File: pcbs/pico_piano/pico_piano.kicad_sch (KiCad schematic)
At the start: 22 parts, among them U1 Pico

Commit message: WIP: real hardware tests
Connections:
- net A: now also U1.24 (GPIO18); no longer U1.22 (GPIO17)
- net AIS: now also U1.22 (GPIO17); no longer U1.24 (GPIO18)
- net B: now also U1.21 (GPIO16); no longer U1.25 (GPIO19)
- net GIS: now also U1.25 (GPIO19); no longer U1.21 (GPIO16)
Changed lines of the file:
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@@
 	)
 	(label "A"
-		(at 91.44 113.03 0)
+		(at 91.44 107.95 0)
 		(fields_autoplaced yes)
 		(effects
@@
 	)
 	(label "GIS"
-		(at 91.44 115.57 0)
+		(at 91.44 105.41 0)
 		(fields_autoplaced yes)
 		(effects
@@
 	)
 	(label "AIS"
-		(at 91.44 107.95 0)
+		(at 91.44 113.03 0)
 		(fields_autoplaced yes)
 		(effects
@@
 	)
 	(label "B"
-		(at 91.44 105.41 0)
+		(at 91.44 115.57 0)
 		(fields_autoplaced yes)
 		(effects

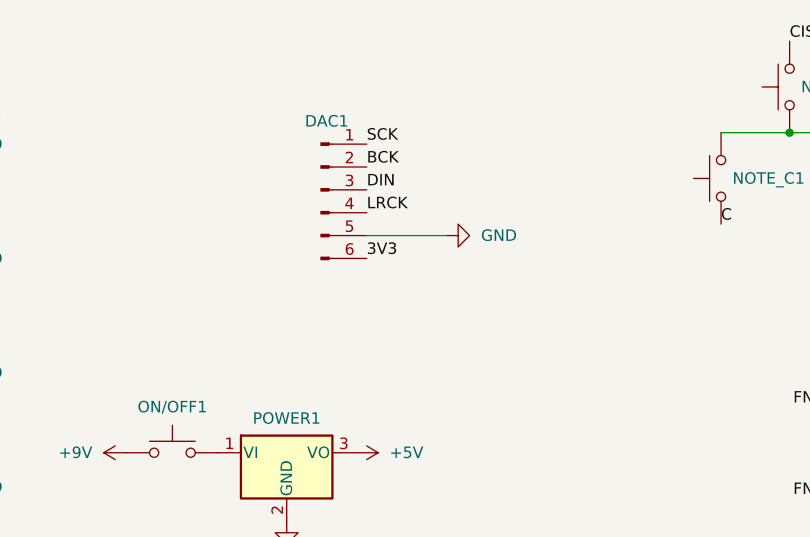
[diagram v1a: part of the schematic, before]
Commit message: Pico Piano PCB changes
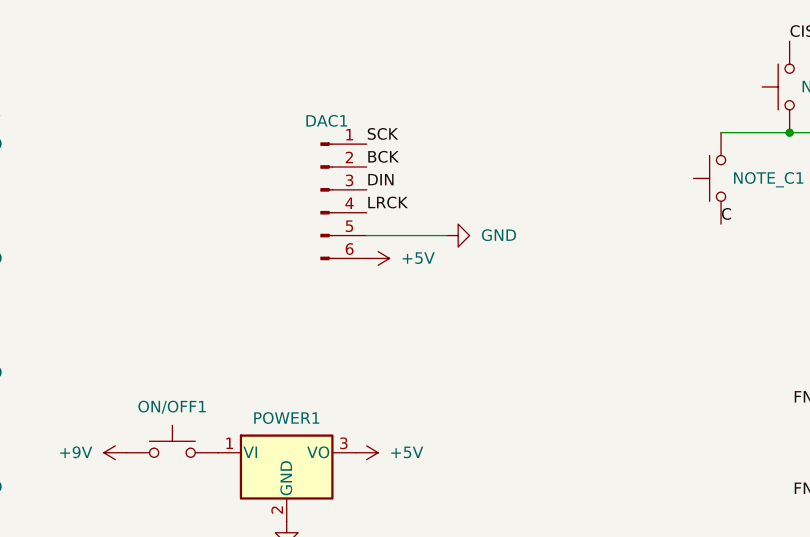
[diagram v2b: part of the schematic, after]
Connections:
- net +5V: now also DAC1.6 (Pin_6)
- net 3V3: no longer DAC1.6 (Pin_6)
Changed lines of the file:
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@@
 		)
 	)
-	(label "3V3"
-		(at 139.7 85.09 0)
+	(label "G"
+		(at 55.88 115.57 180)
 		(fields_autoplaced yes)
 		(effects
@@
 				(size 1.27 1.27)
 			)
-			(justify left bottom)
-		)
-	)
-	(label "G"
-		(at 55.88 115.57 180)
+			(justify right bottom)
+		)
+	)
+	(label "DIS"
+		(at 201.93 60.96 0)
 		(fields_autoplaced yes)
 		(effects
@@
 				(size 1.27 1.27)
 			)
-			(justify right bottom)
-		)
-	)
-	(label "DIS"
-		(at 201.93 60.96 0)
+			(justify left bottom)
+		)
+	)
+	(label "AIS"
+		(at 264.16 60.96 0)
 		(fields_autoplaced yes)
 		(effects
@@
 		)
 	)
-	(label "AIS"
-		(at 264.16 60.96 0)
+	(label "FIS"
+		(at 233.68 60.96 0)
 		(fields_autoplaced yes)
 		(effects
@@
 	)
 	(label "FIS"
-		(at 233.68 60.96 0)
+		(at 55.88 113.03 180)
 		(fields_autoplaced yes)
 		(effects
@@
 				(size 1.27 1.27)
 			)
-			(justify left bottom)
-		)
-	)
-	(label "FIS"
-		(at 55.88 113.03 180)
-		(fields_autoplaced yes)
-		(effects
-			(font
-				(size 1.27 1.27)
-			)
 			(justify right bottom)
 		)
@@
 					(unit 1)
 				)
+			)
+		)
+	)
+	(symbol
+		(lib_id "power:+5V")
+		(at 139.7 85.09 270)
+		(unit 1)
+		(exclude_from_sim no)
+		(in_bom yes)
+		(on_board yes)
+		(dnp no)
+		(fields_autoplaced yes)
+		(property "Reference" "#PWR018"
+			(at 135.89 85.09 0)
+			(effects
+				(font
+					(size 1.27 1.27)
+				)
+				(hide yes)
+			)
+		)
+		(property "Value" "+5V"
+			(at 143.51 85.0899 90)
+			(effects
+				(font
+					(size 1.27 1.27)
+				)
+				(justify left)
+			)
+		)
+		(property "Footprint" ""
+			(at 139.7 85.09 0)
+			(effects
+				(font
+					(size 1.27 1.27)
+				)
+				(hide yes)
+			)
+		)
+		(property "Datasheet" ""
+			(at 139.7 85.09 0)
+			(effects
+				(font
+					(size 1.27 1.27)
+				)
+				(hide yes)
+			)
+		)
+		(property "Description" "Power symbol creates a global label with name \"+5V\""
+			(at 139.7 85.09 0)
+			(effects
+				(font
+					(size 1.27 1.27)
+				)
+				(hide yes)
+			)
+		)
+		(pin "1"
+		)
+		(instances
+			(project ""
+				(path "/5e24b6d7-8d67-4f70-8e44-f3ac3114fe70"
+					(reference "#PWR018")
+					(unit 1)
+				)

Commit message: Update pico piano PCB
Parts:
- POWER1: footprint Package_TO_SOT_THT:TO-220-3_Vertical -> Package_TO_SOT_THT:TO-220-3_Horizontal_TabDown
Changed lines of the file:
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@@
 			)
 		)
-		(property "Footprint" "Package_TO_SOT_THT:TO-220-3_Vertical"
+		(property "Footprint" "Package_TO_SOT_THT:TO-220-3_Horizontal_TabDown"
 			(at 130.81 100.965 0)
 			(effects

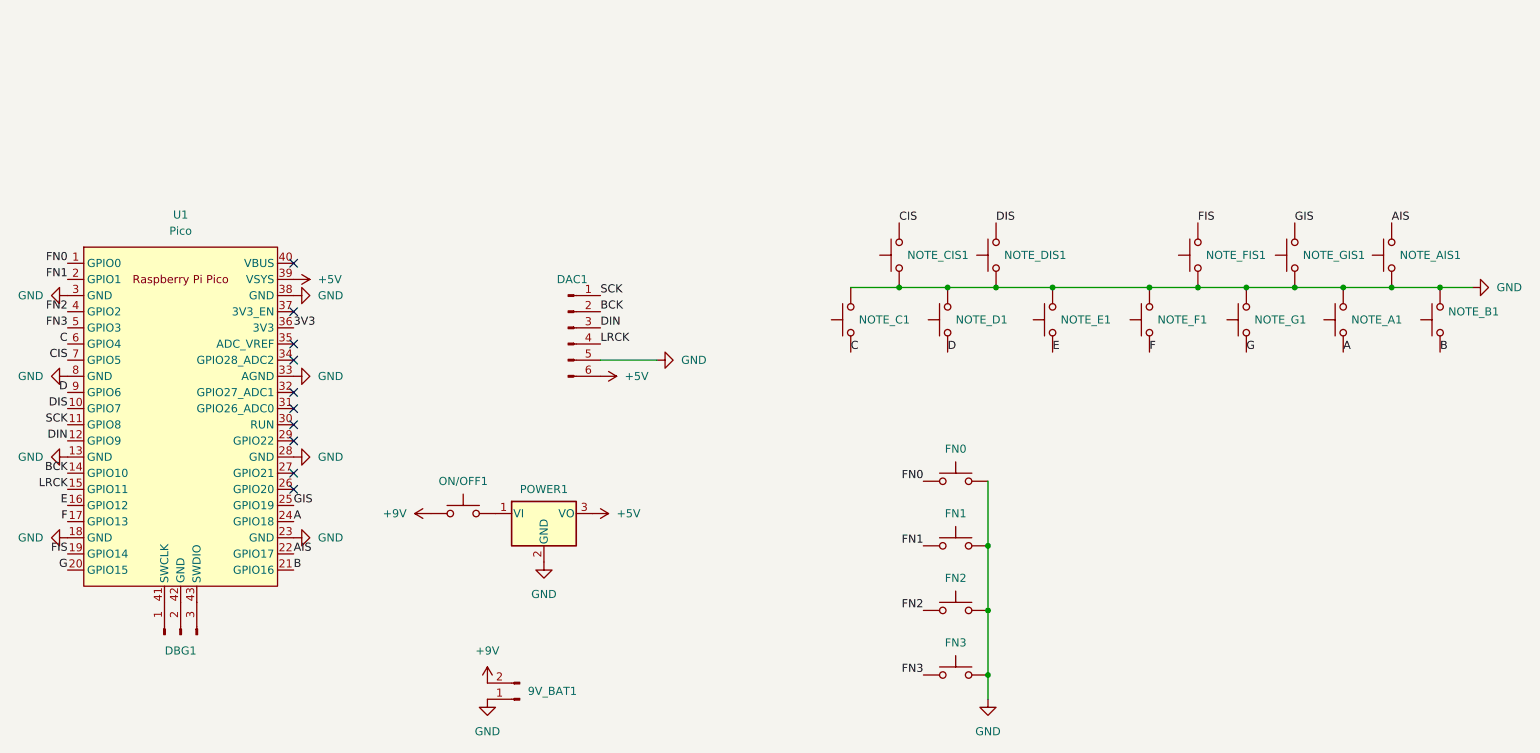
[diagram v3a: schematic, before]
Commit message: Update Pico Piano PCB components
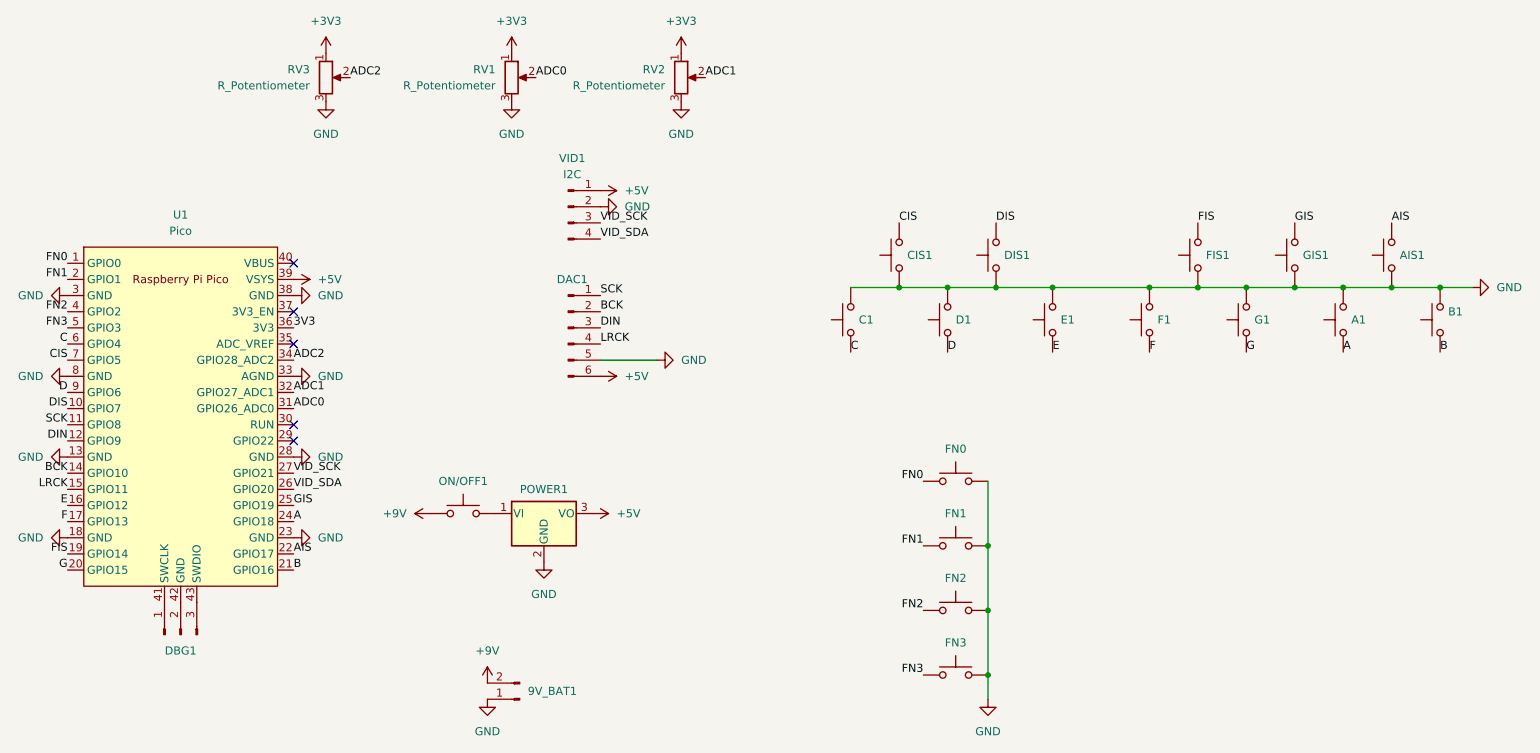
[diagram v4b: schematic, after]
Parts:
- added RV1, RV2, RV3: R_Potentiometer, Connector_PinHeader_2.54mm:PinHeader_1x03_P2.54mm_Vertical, symbol Device:R_Potentiometer
- added VID1: I2C, Connector_PinHeader_2.54mm:PinHeader_1x04_P2.54mm_Vertical, symbol Connector:Conn_01x04_Pin
- A1: renamed from NOTE_A1; footprint Button_Switch_THT:SW_PUSH_6mm -> rytmos:KAILH_MUTE
- AIS1: renamed from NOTE_AIS1; footprint Button_Switch_THT:SW_PUSH_6mm -> rytmos:KAILH_MUTE
- B1: renamed from NOTE_B1; footprint Button_Switch_THT:SW_PUSH_6mm -> rytmos:KAILH_MUTE
- C1: renamed from NOTE_C1; footprint Button_Switch_THT:SW_PUSH_6mm -> rytmos:KAILH_MUTE
- CIS1: renamed from NOTE_CIS1; footprint Button_Switch_THT:SW_PUSH_6mm -> rytmos:KAILH_MUTE
- D1: renamed from NOTE_D1; footprint Button_Switch_THT:SW_PUSH_6mm -> rytmos:KAILH_MUTE
- DIS1: renamed from NOTE_DIS1; footprint Button_Switch_THT:SW_PUSH_6mm -> rytmos:KAILH_MUTE
- E1: renamed from NOTE_E1; footprint Button_Switch_THT:SW_PUSH_6mm -> rytmos:KAILH_MUTE
- F1: renamed from NOTE_F1; footprint Button_Switch_THT:SW_PUSH_6mm -> rytmos:KAILH_MUTE
- FIS1: renamed from NOTE_FIS1; footprint Button_Switch_THT:SW_PUSH_6mm -> rytmos:KAILH_MUTE
- FN0, FN1, FN2, FN3: footprint Button_Switch_THT:SW_PUSH_6mm -> rytmos:KAILH_MUTE
- G1: renamed from NOTE_G1; footprint Button_Switch_THT:SW_PUSH_6mm -> rytmos:KAILH_MUTE
- GIS1: renamed from NOTE_GIS1; footprint Button_Switch_THT:SW_PUSH_6mm -> rytmos:KAILH_MUTE
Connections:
- net +5V: now also VID1.1 (Pin_1)
- net GND: now also RV1.3, RV2.3, RV3.3, VID1.2 (Pin_2)
- net VID_SDA: now reaches U1.26 (GPIO20)
- net VID_SDA: now also VID1.4 (Pin_4)
- net VID_SCK: now reaches U1.27 (GPIO21)
- net VID_SCK: now also VID1.3 (Pin_3)
- net ADC0: now reaches U1.31 (GPIO26_ADC0)
- net ADC0: now also RV1.2
- net ADC1: now reaches U1.32 (GPIO27_ADC1)
- net ADC1: now also RV2.2
- net ADC2: now reaches U1.34 (GPIO28_ADC2)
- net ADC2: now also RV3.2
- new net +3V3: RV1.1, RV2.1, RV3.1
- no-connect marks 10 -> 5

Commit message: Route tracks on pico piano v0.2
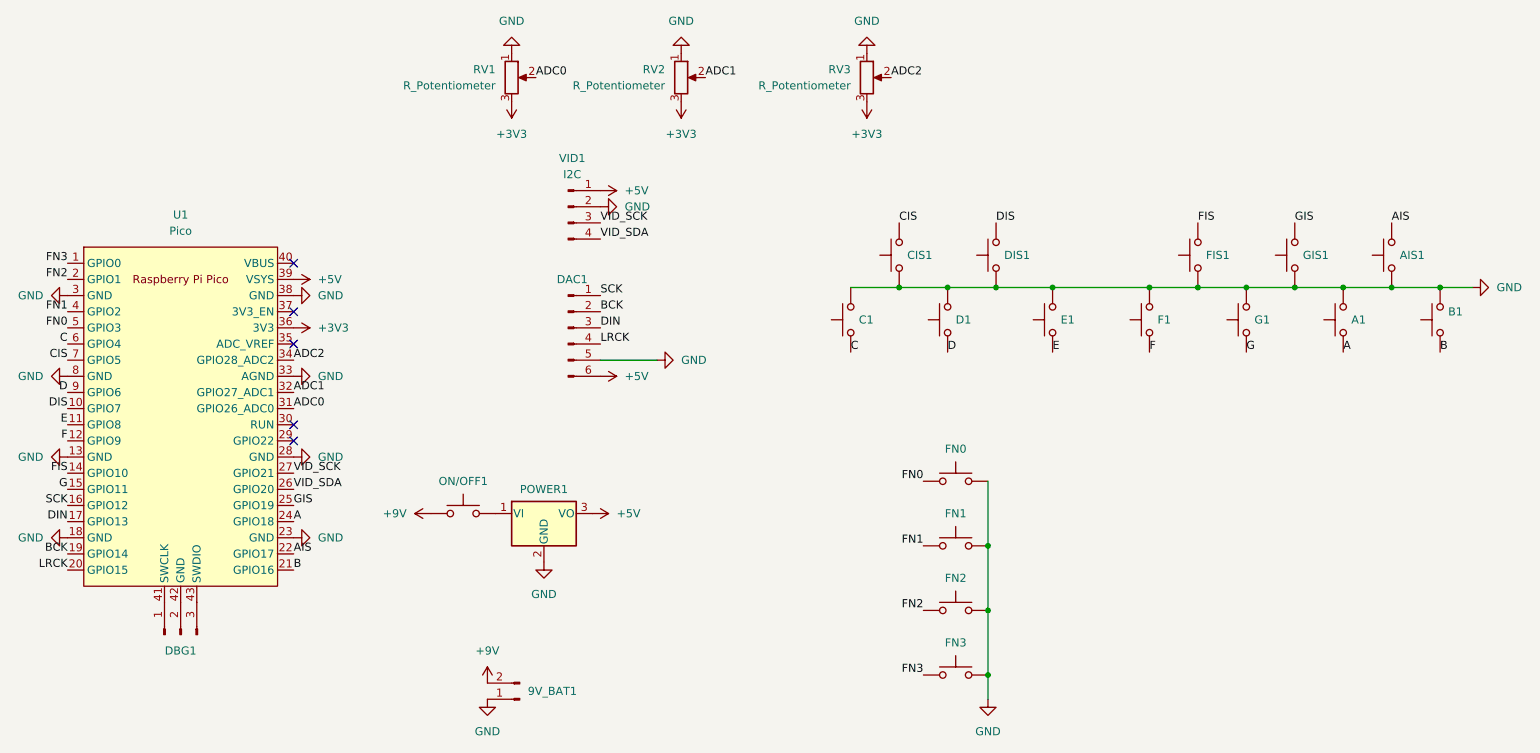
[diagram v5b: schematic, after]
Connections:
- net 3V3 is gone; now on net +3V3: U1.36 (3V3)
- net +3V3: now also RV1.3, RV2.3, RV3.3; no longer RV1.1, RV2.1, RV3.1
- net BCK: now also U1.19 (GPIO14); no longer U1.14 (GPIO10)
- net DIN: now also U1.17 (GPIO13); no longer U1.12 (GPIO9)
- net E: now also U1.11 (GPIO8); no longer U1.16 (GPIO12)
- net F: now also U1.12 (GPIO9); no longer U1.17 (GPIO13)
- net FIS: now also U1.14 (GPIO10); no longer U1.19 (GPIO14)
- net FN0: now also U1.5 (GPIO3); no longer U1.1 (GPIO0)
- net FN1: now also U1.4 (GPIO2); no longer U1.2 (GPIO1)
- net FN2: now also U1.2 (GPIO1); no longer U1.4 (GPIO2)
- net FN3: now also U1.1 (GPIO0); no longer U1.5 (GPIO3)
- net G: now also U1.15 (GPIO11); no longer U1.20 (GPIO15)
- net GND: now also RV1.1, RV2.1, RV3.1; no longer RV1.3, RV2.3, RV3.3
- net LRCK: now also U1.20 (GPIO15); no longer U1.15 (GPIO11)
- net SCK: now also U1.16 (GPIO12); no longer U1.11 (GPIO8)
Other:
- moved on the sheet: RV3
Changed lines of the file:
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@@
 	)
 	(label "SCK"
-		(at 55.88 92.71 180)
+		(at 55.88 105.41 180)
 		(fields_autoplaced yes)
 		(effects
@@
 	)
 	(label "FN3"
-		(at 55.88 77.47 180)
+		(at 55.88 67.31 180)
 		(fields_autoplaced yes)
 		(effects
@@
 	)
 	(label "FN0"
-		(at 55.88 67.31 180)
+		(at 55.88 77.47 180)
 		(fields_autoplaced yes)
 		(effects
@@
 	)
 	(label "F"
-		(at 55.88 107.95 180)
+		(at 55.88 95.25 180)
 		(fields_autoplaced yes)
 		(effects
@@
 	)
 	(label "E"
-		(at 55.88 105.41 180)
+		(at 55.88 92.71 180)
 		(fields_autoplaced yes)
 		(effects
@@
 	)
 	(label "LRCK"
-		(at 55.88 102.87 180)
+		(at 55.88 115.57 180)
 		(fields_autoplaced yes)
 		(effects
@@
 	)
 	(label "FN2"
-		(at 55.88 74.93 180)
+		(at 55.88 69.85 180)
 		(fields_autoplaced yes)
 		(effects
@@
 	)
 	(label "FN1"
-		(at 55.88 69.85 180)
+		(at 55.88 74.93 180)
 		(fields_autoplaced yes)
 		(effects
@@
 	)
 	(label "BCK"
-		(at 55.88 100.33 180)
+		(at 55.88 113.03 180)
 		(fields_autoplaced yes)
 		(effects
@@
 	)
 	(label "DIN"
-		(at 55.88 95.25 180)
+		(at 55.88 107.95 180)
 		(fields_autoplaced yes)
 		(effects
@@
 		)
 	)
-	(label "3V3"
-		(at 91.44 77.47 0)
-		(fields_autoplaced yes)
-		(effects
-			(font
-				(size 1.27 1.27)
-			)
-			(justify left bottom)
-		)
-	)
 	(label "D"
 		(at 194.31 81.28 0)
@@
 	)
 	(label "G"
-		(at 55.88 115.57 180)
+		(at 55.88 102.87 180)
 		(fields_autoplaced yes)
 		(effects
@@
 	)
 	(label "FIS"
-		(at 55.88 113.03 180)
+		(at 55.88 100.33 180)
 		(fields_autoplaced yes)
 		(effects
@@
 	)
 	(label "ADC2"
-		(at 100.33 38.1 0)
+		(at 185.42 38.1 0)
 		(fields_autoplaced yes)
 		(effects
@@
 	(symbol
 		(lib_id "power:+3V3")
-		(at 96.52 34.29 0)
+		(at 125.73 41.91 180)
 		(unit 1)
 		(exclude_from_sim no)
@@
 		(fields_autoplaced yes)
 		(property "Reference" "#PWR019"
-			(at 96.52 38.1 0)
+			(at 125.73 38.1 0)
 			(effects
 				(font
@@
 		)
 		(property "Value" "+3V3"
-			(at 96.52 29.21 0)
+			(at 125.73 46.99 0)
 			(effects
 				(font
@@
 		)
 		(property "Footprint" ""
-			(at 96.52 34.29 0)
+			(at 125.73 41.91 0)
 			(effects
 				(font
@@
 		)
 		(property "Datasheet" ""
-			(at 96.52 34.29 0)
+			(at 125.73 41.91 0)
 			(effects
 				(font
@@
 		)
 		(property "Description" "Power symbol creates a global label with name \"+3V3\""
-			(at 96.52 34.29 0)
+			(at 125.73 41.91 0)
 			(effects
 				(font
@@
 	(symbol
 		(lib_id "power:+3V3")
-		(at 125.73 34.29 0)
+		(at 181.61 41.91 180)
 		(unit 1)
 		(exclude_from_sim no)
@@
 		(fields_autoplaced yes)
 		(property "Reference" "#PWR021"
-			(at 125.73 38.1 0)
+			(at 181.61 38.1 0)
 			(effects
 				(font
@@
 		)
 		(property "Value" "+3V3"
-			(at 125.73 29.21 0)
+			(at 181.61 46.99 0)
 			(effects
 				(font
@@
 		)
 		(property "Footprint" ""
-			(at 125.73 34.29 0)
+			(at 181.61 41.91 0)
 			(effects
 				(font
@@
 		)
 		(property "Datasheet" ""
-			(at 125.73 34.29 0)
+			(at 181.61 41.91 0)
 			(effects
 				(font
@@
 		)
 		(property "Description" "Power symbol creates a global label with name \"+3V3\""
-			(at 125.73 34.29 0)
+			(at 181.61 41.91 0)
 			(effects
 				(font
@@
 	(symbol
 		(lib_id "power:GND")
-		(at 96.52 41.91 0)
+		(at 125.73 34.29 180)
 		(unit 1)
 		(exclude_from_sim no)
@@
 		(fields_autoplaced yes)
 		(property "Reference" "#PWR020"
-			(at 96.52 48.26 0)
+			(at 125.73 27.94 0)
 			(effects
 				(font
@@
 		)
 		(property "Value" "GND"
-			(at 96.52 46.99 0)
+			(at 125.73 29.21 0)
 			(effects
 				(font
@@
 		)
 		(property "Footprint" ""
-			(at 96.52 41.91 0)
+			(at 125.73 34.29 0)
 			(effects
 				(font
@@
 		)
 		(property "Datasheet" ""
-			(at 96.52 41.91 0)
+			(at 125.73 34.29 0)
 			(effects
 				(font
@@
 		)
 		(property "Description" "Power symbol creates a global label with name \"GND\" , ground"
-			(at 96.52 41.91 0)
+			(at 125.73 34.29 0)
 			(effects
 				(font
@@
 	(symbol
 		(lib_id "power:GND")
-		(at 152.4 41.91 0)
+		(at 152.4 34.29 180)
 		(unit 1)
 		(exclude_from_sim no)
@@
 		(fields_autoplaced yes)
 		(property "Reference" "#PWR024"
-			(at 152.4 48.26 0)
+			(at 152.4 27.94 0)
 			(effects
 				(font
@@
 		)
 		(property "Value" "GND"
-			(at 152.4 46.99 0)
+			(at 152.4 29.21 0)
 			(effects
 				(font
@@
 		)
 		(property "Footprint" ""
-			(at 152.4 41.91 0)
+			(at 152.4 34.29 0)
 			(effects
 				(font
@@
 		)
 		(property "Datasheet" ""
-			(at 152.4 41.91 0)
+			(at 152.4 34.29 0)
 			(effects
 				(font
@@
 		)
 		(property "Description" "Power symbol creates a global label with name \"GND\" , ground"
-			(at 152.4 41.91 0)
+			(at 152.4 34.29 0)
 			(effects
 				(font
@@
 	(symbol
 		(lib_id "power:+3V3")
-		(at 152.4 34.29 0)
+		(at 152.4 41.91 180)
 		(unit 1)
 		(exclude_from_sim no)
@@
 		)
 		(property "Value" "+3V3"
-			(at 152.4 29.21 0)
+			(at 152.4 46.99 0)
 			(effects
 				(font
@@
 		)
 		(property "Footprint" ""
-			(at 152.4 34.29 0)
+			(at 152.4 41.91 0)
 			(effects
 				(font
@@
 		)
 		(property "Datasheet" ""
-			(at 152.4 34.29 0)
+			(at 152.4 41.91 0)
 			(effects
 				(font
@@
 		)
 		(property "Description" "Power symbol creates a global label with name \"+3V3\""
-			(at 152.4 34.29 0)
+			(at 152.4 41.91 0)
 			(effects
 				(font
@@
 	)
 	(symbol
+		(lib_id "power:+3V3")
+		(at 91.44 77.47 270)
+		(unit 1)
+		(exclude_from_sim no)
+		(in_bom yes)
+		(on_board yes)
+		(dnp no)
+		(fields_autoplaced yes)
+		(property "Reference" "#PWR027"
+			(at 87.63 77.47 0)
+			(effects
+				(font
+					(size 1.27 1.27)
+				)
+				(hide yes)
+			)
+		)
+		(property "Value" "+3V3"
+			(at 95.25 77.4699 90)
+			(effects
+				(font
+					(size 1.27 1.27)
+				)
+				(justify left)
+			)
+		)
+		(property "Footprint" ""
+			(at 91.44 77.47 0)
+			(effects
+				(font
+					(size 1.27 1.27)
+				)
+				(hide yes)
+			)
+		)
+		(property "Datasheet" ""
+			(at 91.44 77.47 0)
+			(effects
+				(font
+					(size 1.27 1.27)
+				)
+				(hide yes)
+			)
+		)
+		(property "Description" "Power symbol creates a global label with name \"+3V3\""
+			(at 91.44 77.47 0)
+			(effects
+				(font
+					(size 1.27 1.27)
+				)
+				(hide yes)
+			)
+		)
+		(pin "1"
+		)
+		(instances
+			(project ""
+				(path "/5e24b6d7-8d67-4f70-8e44-f3ac3114fe70"
+					(reference "#PWR027")
+					(unit 1)
+				)
+			)
+		)
+	)
+	(symbol
 		(lib_id "Device:R_Potentiometer")
-		(at 96.52 38.1 0)
+		(at 181.61 38.1 0)
 		(unit 1)
 		(exclude_from_sim no)
@@
 		(fields_autoplaced yes)
 		(property "Reference" "RV3"
-			(at 93.98 36.8299 0)
+			(at 179.07 36.8299 0)
 			(effects
 				(font
@@
 		)
 		(property "Value" "R_Potentiometer"
-			(at 93.98 39.3699 0)
+			(at 179.07 39.3699 0)
 			(effects
 				(font
@@
 		)
 		(property "Footprint" "Connector_PinHeader_2.54mm:PinHeader_1x03_P2.54mm_Vertical"
-			(at 96.52 38.1 0)
+			(at 181.61 38.1 0)
 			(effects
 				(font
@@
 		)
 		(property "Datasheet" "~"
-			(at 96.52 38.1 0)
+			(at 181.61 38.1 0)
 			(effects
 				(font
@@
 		)
 		(property "Description" "Potentiometer"
-			(at 96.52 38.1 0)
+			(at 181.61 38.1 0)
 			(effects
 				(font
@@
 	(symbol
 		(lib_id "power:GND")
-		(at 125.73 41.91 0)
+		(at 181.61 34.29 180)
 		(unit 1)
 		(exclude_from_sim no)
@@
 		(fields_autoplaced yes)
 		(property "Reference" "#PWR022"
-			(at 125.73 48.26 0)
+			(at 181.61 27.94 0)
 			(effects
 				(font
@@
 		)
 		(property "Value" "GND"
-			(at 125.73 46.99 0)
+			(at 181.61 29.21 0)
 			(effects
 				(font
@@
 		)
 		(property "Footprint" ""
-			(at 125.73 41.91 0)
+			(at 181.61 34.29 0)
 			(effects
 				(font
@@
 		)
 		(property "Datasheet" ""
-			(at 125.73 41.91 0)
+			(at 181.61 34.29 0)
 			(effects
 				(font
@@
 		)
 		(property "Description" "Power symbol creates a global label with name \"GND\" , ground"
-			(at 125.73 41.91 0)
+			(at 181.61 34.29 0)
 			(effects
 				(font
